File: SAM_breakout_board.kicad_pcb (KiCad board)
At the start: 2 copper layers, 50.3 x 50.3 mm, 56 parts, among them J1 Conn_01x04, J10 Conn_01x12, J11 Conn_01x12, J2 Conn_01x04, J3 Conn_01x02, J4 USB_B_Micro, J5 Conn_ARM_JTAG_SWD_10, J6 Conn_01x04, J7 Conn_01x04, J8 Conn_01x02, J9 Conn_01x12, SW1 BATT_PWR, SW2 RST_SW, SW3 MAIN_PWR, U1 TPS62163DSG, U2 TPS63060, U3 ATSAMD21G18A-AUT, Y1 Crystal_ABS

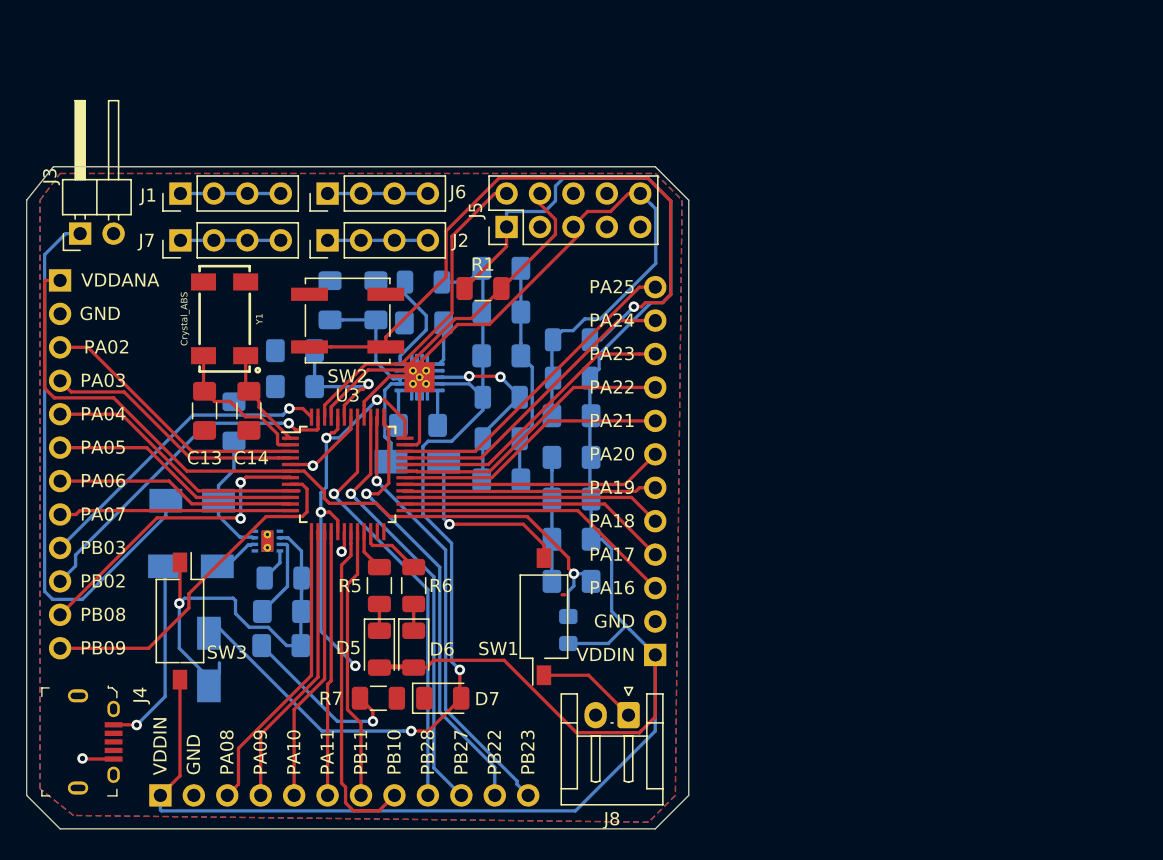
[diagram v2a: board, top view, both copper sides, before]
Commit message: Rearranged layout completely
Board is done with the exception of validation.
PCB will be in on 10/28/2019.

Added a BOM for ordering, will be continually modifying as needed.
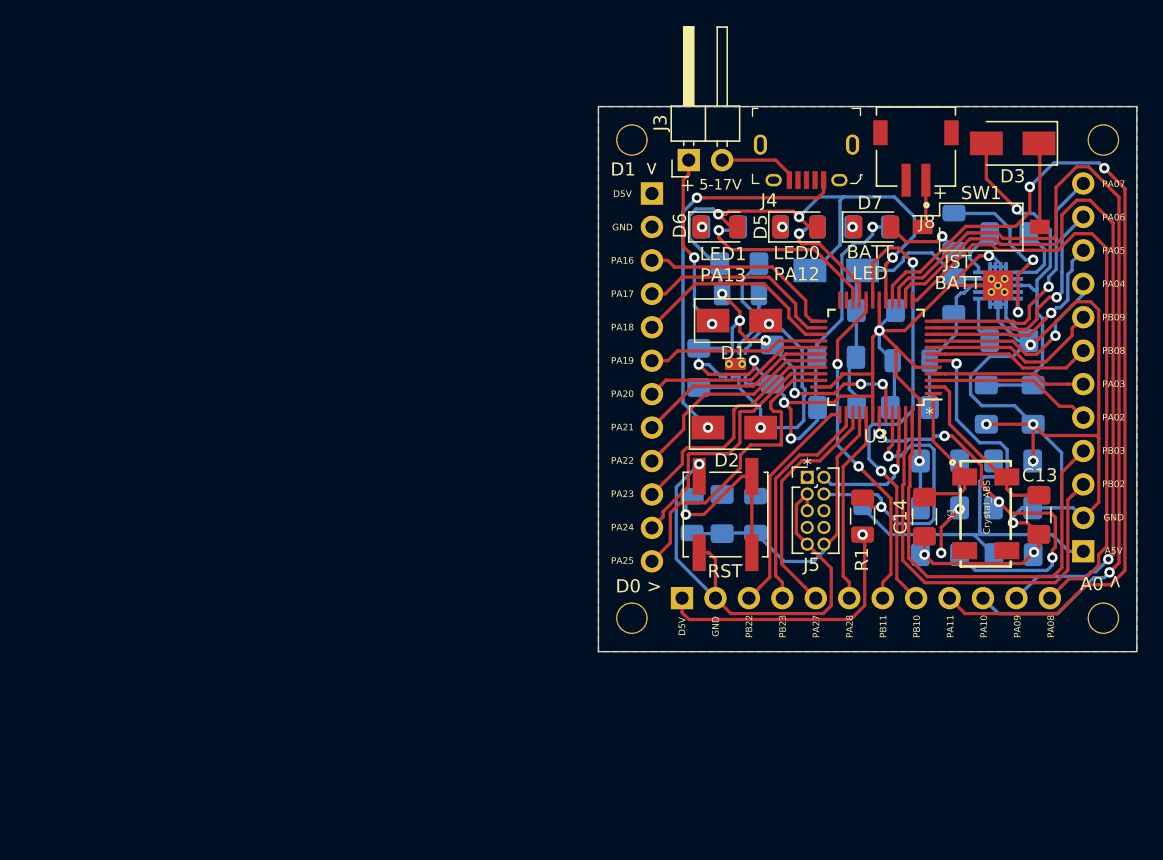
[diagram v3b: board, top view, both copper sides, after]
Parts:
- removed J1, J2, J6, J7: Conn_01x04, Connector_PinHeader_2.54mm:PinHeader_1x04_P2.54mm_Vertical
- removed SW2: RST_SW, Button_Switch_SMD:SW_Push_1P1T_NO_CK_KSC6xxJ
- removed SW3: MAIN_PWR, Button_Switch_SMD:SW_DIP_SPSTx01_Slide_Omron_A6S-110x_W8.9mm_P2.54mm
- added REF**: MountingHole_2.2mm_M2, MountingHole:MountingHole_2.2mm_M2, F.Cu at (167.4, 102.4)
- added REF**: MountingHole_2.2mm_M2, MountingHole:MountingHole_2.2mm_M2, F.Cu at (203.2, 102.4)
- added REF**: MountingHole_2.2mm_M2, MountingHole:MountingHole_2.2mm_M2, F.Cu at (203.2, 66.0)
- added REF**: MountingHole_2.2mm_M2, MountingHole:MountingHole_2.2mm_M2, F.Cu at (167.4, 66.0)
- added RST: RST_SW, Button_Switch_SMD:SW_Push_1P1T_NO_CK_KSC6xxJ, F.Cu at (174.5, 94.5)
- D1, D2, D3: moved to F.Cu
- J5: footprint Connector_PinHeader_2.54mm:PinHeader_2x05_P2.54mm_Vertical -> Connector_PinHeader_1.27mm:PinHeader_2x05_P1.27mm_Vertical
- J8: footprint Connector_JST:JST_EH_S2B-EH_1x02_P2.50mm_Horizontal -> S2B-ZR-SM4A-TF_LF__SN_:JST_S2B-ZR-SM4A-TF(LF)(SN)
- R5, R6, R7: moved to B.Cu
- moved J9 80.4 mm to (201.7, 97.3), turned to 0 degrees
- moved J4 67.8 mm to (180.7, 69.1), turned to 180 degrees
- moved C13 63.9 mm to (198.3, 94.5)
- moved Y1 59.7 mm to (194.3, 94.4), turned to 270 degrees
- moved D4 56.1 mm to (182.9, 75.9), turned to 180 degrees
- moved C9 55.8 mm to (196.3, 94.0), turned to 0 degrees
- moved C14 51.9 mm to (189.6, 94.7)
- moved R7 51.8 mm to (185.5, 72.6), turned to 0 degrees
- moved D3 51.3 mm to (196.3, 66.3)
- moved C8 50.6 mm to (190.8, 97.5)
- moved C10 50.5 mm to (197.9, 86.1), turned to 270 degrees
- moved C11 50.5 mm to (194.3, 86.1), turned to 270 degrees
- moved D7 48.5 mm to (185.7, 72.6)
- moved J8 48.0 mm to (189.0, 66.9)
- moved L2 47.2 mm to (196.1, 73.2), turned to 180 degrees
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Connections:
- C3 pad 1: Net-(C3-Pad1) -> VDDIN
- D4 pad 2: Net-(C3-Pad1) -> VDDIN
- J10 pad 10: PA27 -> PA10
- J10 pad 11: PB22 -> PA09
- J10 pad 12: PB23 -> PA08
- J10 pad 3: PA08 -> PB22
- J10 pad 4: PA09 -> PB23
- J10 pad 5: PA10 -> PA27
- J10 pad 6: PA11 -> PA28
- J10 pad 9: PA28 -> PA11
- J9 pad 10: PB02 -> PA05
- J9 pad 11: PB08 -> PA06
- J9 pad 12: PB09 -> PA07
- J9 pad 3: PA02 -> PB02
- J9 pad 4: PA03 -> PB03
- J9 pad 5: PA04 -> PA02
- J9 pad 6: PA05 -> PA03
- J9 pad 7: PA06 -> PB08
- J9 pad 8: PA07 -> PB09
- J9 pad 9: PB03 -> PA04
- L1 pad 1: Net-(C3-Pad1) -> VDDIN
- R4 pad 2: Net-(C3-Pad1) -> VDDIN
- U1 pad 6: Net-(C3-Pad1) -> VDDIN
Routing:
- net GND: track 56.1 -> 237.1 mm, vias 4 -> 17
- net VDDIN: track 187.3 -> 97.8 mm, vias 4 -> 12
- net PA11: track 20.1 -> 68.7 mm, vias 0 -> 2
- net PA10: track 21.0 -> 65.1 mm, vias 0 -> 1
- net 5V_BATT: track 67.3 -> 29.1 mm, vias 2 -> 1
- net Net-(R3-Pad2): track 50.6 -> 13.2 mm
- net Net-(C3-Pad1): track 34.7 -> 0.00 mm, vias 1 -> 0
- net PA09: track 21.9 -> 55.4 mm, vias 0 -> 1
- net Net-(D1-Pad1): track 42.2 -> 13.9 mm, vias 0 -> 2
- net RST: track 50.3 -> 22.9 mm
- net PA08: track 22.7 -> 46.7 mm
- net VDDANA: track 61.1 -> 39.8 mm
- net VDDCORE: track 10.3 -> 30.0 mm, vias 1 -> 4
- net PA28: track 32.4 -> 14.9 mm, vias 1 -> 0
- net PB22: track 34.2 -> 17.2 mm, vias 1 -> 0
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- added copper zone on B.Cu, net VDDIN
- removed copper zone on B.Cu, net GND
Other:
- board size 50.3 x 50.3 mm -> 40.9 x 41.4 mm
- board text added: "*"
- board text added: "+"
- board text added: "5-17V"
- board text added: ">"
- board text added: "A0"
- board text added: "A5V"
- board text added: "BATT LED"
- board text added: "D0 >"
- board text added: "D1"
- board text added: "D5V"
- board text added: "I2C: PA08,PA09,PA12,PA13 PA16,PA17,PA22,PA23"
- board text added: "JST BATT"
- board text added: "LED0 PA12"
- board text added: "LED1 PA13"
- board text added: "PA27"
- board text added: "PA28"
- board text added: "little_devil V1.0.0 10.22.2019 Chris Johnson & John Wiggins"
- board text removed: "PB27"
- board text removed: "PB28"
- board text removed: "VDDANA"
- board text removed: "VDDIN"
